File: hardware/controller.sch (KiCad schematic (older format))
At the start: 76 parts, among them J1 USB_B_Micro, Q1 AO3402, Q2 AO3401A, Q3 AO3402, SW1 SW_Push_NO_NC_LED, SW10 SW_Push_NO_NC_LED, SW11 SW_Push_NO_NC_LED, SW12 SW_Push_NO_NC_LED, SW13 SW_Push_NO_NC_LED, SW14 SW_Push_NO_NC_LED, SW15 SW_Push_NO_NC_LED, SW16 SW_Push_NO_NC_LED, SW2 SW_Push_NO_NC_LED, SW3 SW_Push_NO_NC_LED, SW4 SW_Push_NO_NC_LED, SW5 SW_Push_NO_NC_LED, SW6 SW_Push_NO_NC_LED, SW7 SW_Push_NO_NC_LED, SW8 SW_Push_NO_NC_LED, SW9 SW_Push_NO_NC_LED, U1 ESP-12F, U2 ME6211C33M5G, U3 MCP23017_SS, U4 CH340C, U5 PCA9685PW

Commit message: rename files, update library references
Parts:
- SW1, SW10, SW11, SW12, SW13, SW14, SW15, SW16, SW2, SW3, SW4, SW5, SW6, SW7, SW8, SW9: symbol ledcontrol:SW_Push_NO_NC_LED -> controller:SW_Push_NO_NC_LED
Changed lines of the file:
@@
 	1150 6750 1550 6750
 $Comp
-L ledcontrol:SW_Push_NO_NC_LED SW1
+L controller:SW_Push_NO_NC_LED SW1
 U 1 1 5F65B435
 P 8650 1600
@@
 NoConn ~ 8400 2050
 $Comp
-L ledcontrol:SW_Push_NO_NC_LED SW2
+L controller:SW_Push_NO_NC_LED SW2
 U 1 1 5F6F8CEF
 P 8650 2250
@@
 NoConn ~ 8400 2700
 $Comp
-L ledcontrol:SW_Push_NO_NC_LED SW3
+L controller:SW_Push_NO_NC_LED SW3
 U 1 1 5F714105
 P 8650 2900
@@
 NoConn ~ 8400 3350
 $Comp
-L ledcontrol:SW_Push_NO_NC_LED SW4
+L controller:SW_Push_NO_NC_LED SW4
 U 1 1 5F714114
 P 8650 3550
@@
 NoConn ~ 8400 4000
 $Comp
-L ledcontrol:SW_Push_NO_NC_LED SW5
+L controller:SW_Push_NO_NC_LED SW5
 U 1 1 5F72F275
 P 8650 4200
@@
 NoConn ~ 8400 4650
 $Comp
-L ledcontrol:SW_Push_NO_NC_LED SW6
+L controller:SW_Push_NO_NC_LED SW6
 U 1 1 5F72F284
 P 8650 4850
@@
 NoConn ~ 8400 5300
 $Comp
-L ledcontrol:SW_Push_NO_NC_LED SW7
+L controller:SW_Push_NO_NC_LED SW7
 U 1 1 5F72F293
 P 8650 5500
@@
 NoConn ~ 8400 5950
 $Comp
-L ledcontrol:SW_Push_NO_NC_LED SW8
+L controller:SW_Push_NO_NC_LED SW8
 U 1 1 5F72F2A2
 P 8650 6150
@@
 NoConn ~ 10050 1400
 $Comp
-L ledcontrol:SW_Push_NO_NC_LED SW9
+L controller:SW_Push_NO_NC_LED SW9
 U 1 1 5E53C282
 P 10300 1600
@@
 NoConn ~ 10050 2050
 $Comp
-L ledcontrol:SW_Push_NO_NC_LED SW10
+L controller:SW_Push_NO_NC_LED SW10
 U 1 1 5E53C28D
 P 10300 2250
@@
 NoConn ~ 10050 2700
 $Comp
-L ledcontrol:SW_Push_NO_NC_LED SW11
+L controller:SW_Push_NO_NC_LED SW11
 U 1 1 5E53C298
 P 10300 2900
@@
 NoConn ~ 10050 3350
 $Comp
-L ledcontrol:SW_Push_NO_NC_LED SW12
+L controller:SW_Push_NO_NC_LED SW12
 U 1 1 5E53C2A3
 P 10300 3550
@@
 NoConn ~ 10050 4000
 $Comp
-L ledcontrol:SW_Push_NO_NC_LED SW13
+L controller:SW_Push_NO_NC_LED SW13
 U 1 1 5E53C2AE
 P 10300 4200
@@
 NoConn ~ 10050 4650
 $Comp
-L ledcontrol:SW_Push_NO_NC_LED SW14
+L controller:SW_Push_NO_NC_LED SW14
 U 1 1 5E53C2B9
 P 10300 4850
@@
 NoConn ~ 10050 5300
 $Comp
-L ledcontrol:SW_Push_NO_NC_LED SW15
+L controller:SW_Push_NO_NC_LED SW15
 U 1 1 5E53C2C4
 P 10300 5500
@@
 NoConn ~ 10050 5950
 $Comp
-L ledcontrol:SW_Push_NO_NC_LED SW16
+L controller:SW_Push_NO_NC_LED SW16
 U 1 1 5E53C2CF
 P 10300 6150

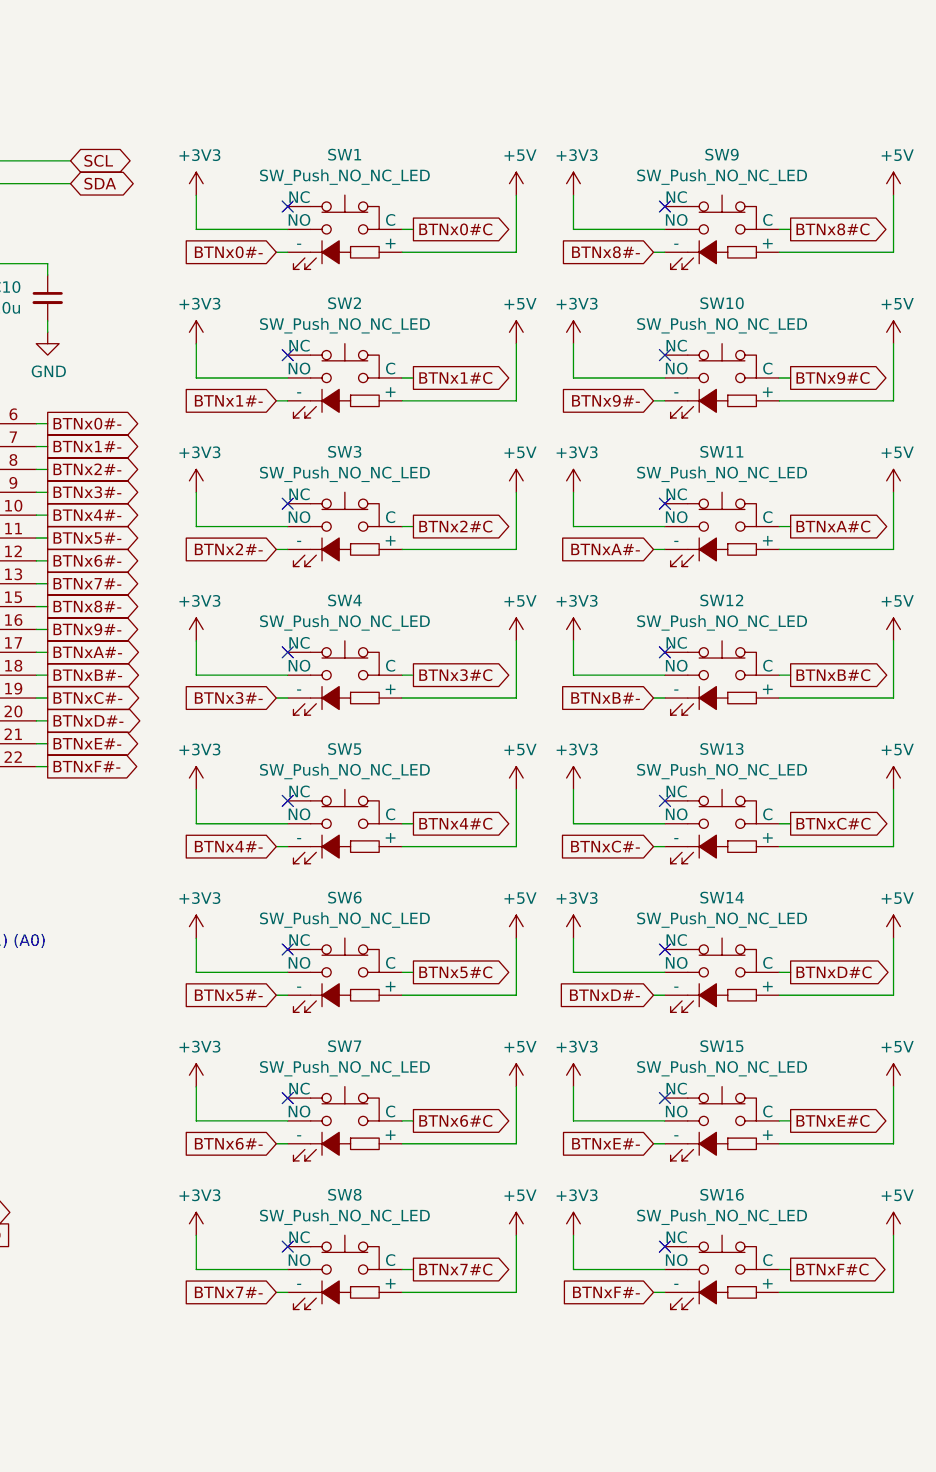
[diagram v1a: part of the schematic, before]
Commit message: connect buttons' NO to GND (MCP23017 has configurable internal pull-up resistors)
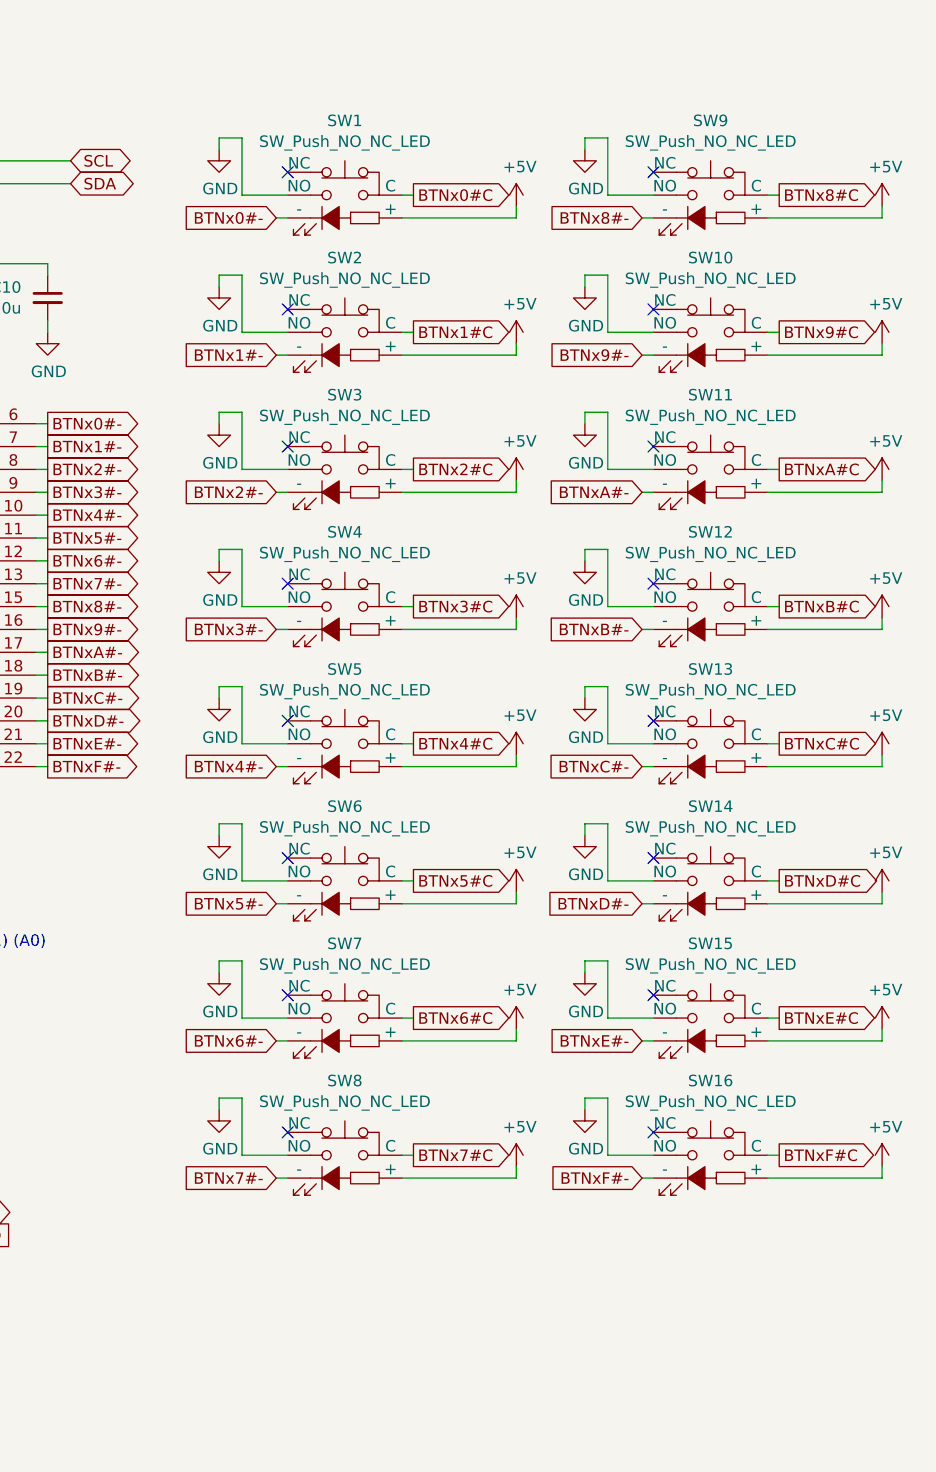
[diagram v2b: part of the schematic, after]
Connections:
- net +3V3: no longer SW1.3 (NO), SW10.3 (NO), SW11.3 (NO), SW12.3 (NO), SW13.3 (NO), SW14.3 (NO), SW15.3 (NO), SW16.3 (NO), SW2.3 (NO), SW3.3 (NO), SW4.3 (NO), SW5.3 (NO), SW6.3 (NO), SW7.3 (NO), SW8.3 (NO), SW9.3 (NO)
- net GND: now also SW1.3 (NO), SW10.3 (NO), SW11.3 (NO), SW12.3 (NO), SW13.3 (NO), SW14.3 (NO), SW15.3 (NO), SW16.3 (NO), SW2.3 (NO), SW3.3 (NO), SW4.3 (NO), SW5.3 (NO), SW6.3 (NO), SW7.3 (NO), SW8.3 (NO), SW9.3 (NO)
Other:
- moved on the sheet: SW1
